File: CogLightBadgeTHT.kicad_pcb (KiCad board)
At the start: 2 copper layers, 87.4 x 123 mm, 28 parts, among them J1 AVR-ISP, SW1 SW_SPDT, SW2 SW_Push, SW3 SW_Push, U1 ATtiny84A-PU

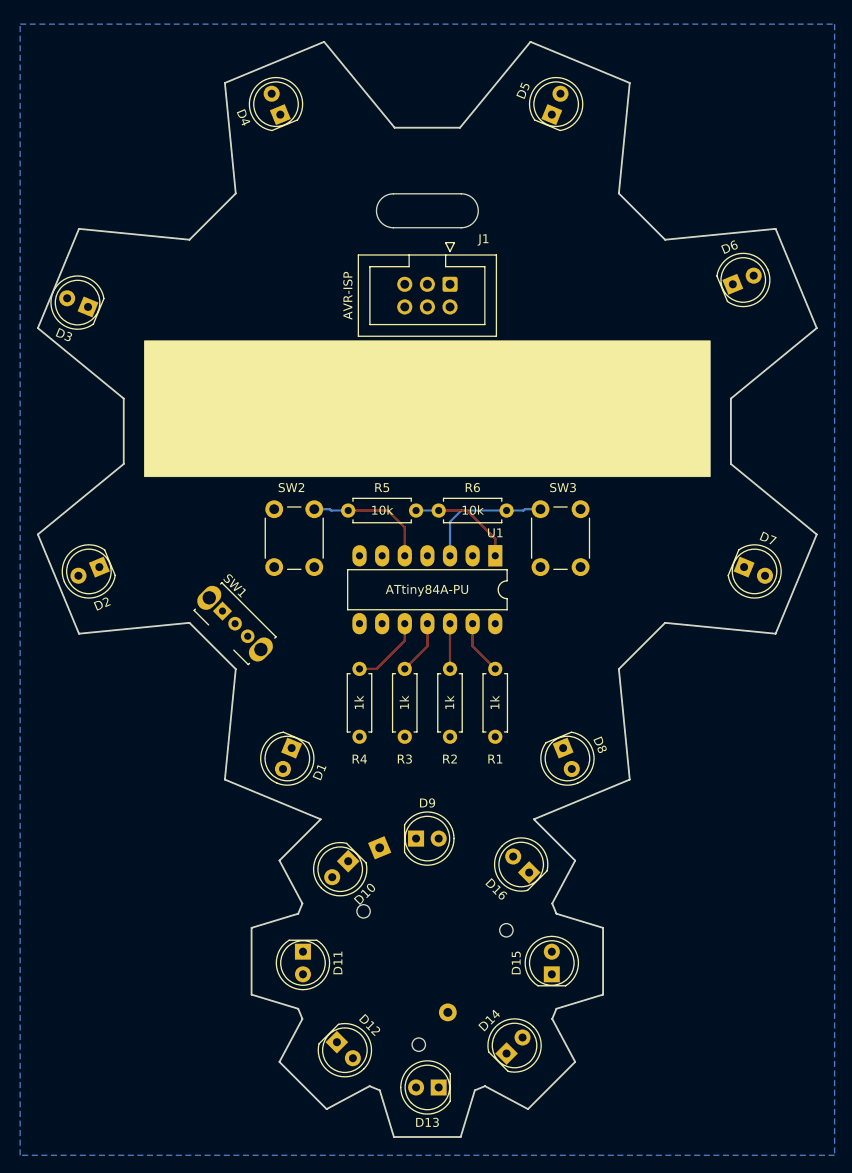
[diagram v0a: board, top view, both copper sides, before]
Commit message: Downsized pcb and component layout
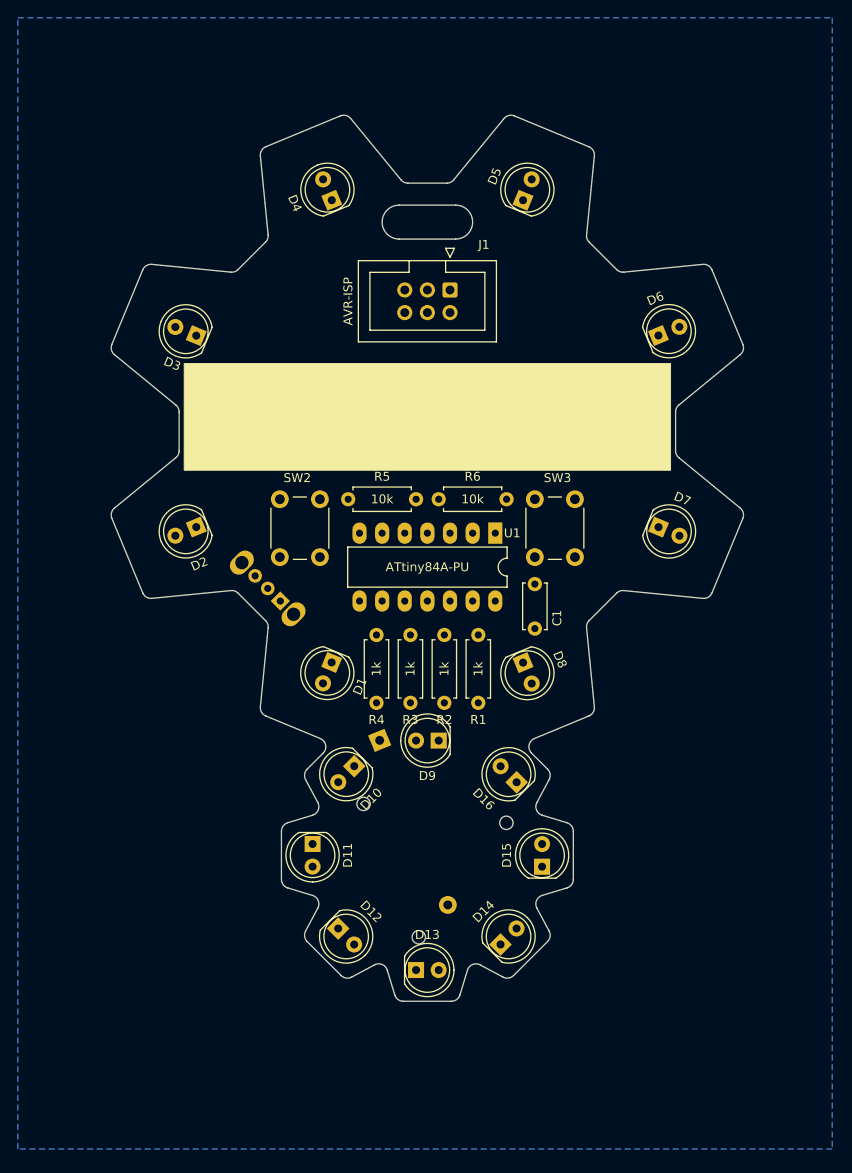
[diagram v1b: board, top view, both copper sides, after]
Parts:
- added C1: 100nF, Capacitor_THT:C_Disc_D5.0mm_W2.5mm_P5.00mm, F.Cu at (88.3, 93.3)
- SW1: moved to B.Cu
- moved D13 13.4 mm to (74.9, 136.7), turned to 0 degrees
- moved D12 12.8 mm to (66.2, 132.0)
- moved D3 12.6 mm to (50.2, 65.5)
- moved D14 12.3 mm to (84.4, 133.8)
- moved D11 12.1 mm to (63.3, 122.5)
- moved D15 12.1 mm to (89.1, 125.1)
- moved BT1 12.1 mm to (76.2, 123.8)
- moved D2 11.8 mm to (50.3, 86.9)
- moved D9 11.3 mm to (77.5, 110.9), turned to 180 degrees
- moved D4 11.2 mm to (65.5, 50.3)
- moved D10 10.7 mm to (68.0, 113.8)
- moved D1 10.6 mm to (65.5, 102.1)
- moved D7 10.6 mm to (102.2, 87.0)
- moved D8 10.6 mm to (86.9, 102.2)
- moved D16 10.2 mm to (86.2, 115.6)
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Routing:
- net Net-(R6-Pad2): track 14.6 -> 0.00 mm
- net Net-(R5-Pad2): track 14.2 -> 0.00 mm
- net VCC: track 12.1 -> 0.00 mm
- net /source4: track 8.30 -> 0.00 mm
- net /source3: track 6.13 -> 0.00 mm
- net /source1: track 6.13 -> 0.00 mm
- net /source2: track 5.08 -> 0.00 mm
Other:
- board size 87.4 x 123 mm -> 71 x 99.5 mm

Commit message: Trace routing
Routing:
- net /sink3: track 0.00 -> 159.2 mm, vias 0 -> 8
- net /sink2: track 0.00 -> 144.8 mm, vias 0 -> 3
- net /sink4: track 0.00 -> 126.9 mm, vias 0 -> 1
- net /sink1: track 0.00 -> 120.5 mm, vias 0 -> 4
- net Net-(D1-Pad2): track 0.00 -> 97.7 mm, vias 0 -> 1
- net Net-(D5-Pad2): track 0.00 -> 84.6 mm
- net VCC: track 0.00 -> 65.3 mm
- net Net-(D13-Pad2): track 0.00 -> 55.9 mm
- net Net-(D10-Pad2): track 0.00 -> 39.8 mm
- net Net-(J1-Pad5): track 0.00 -> 30.0 mm
- net Net-(BT1-Pad1): track 0.00 -> 27.6 mm
- net Net-(R6-Pad2): track 0.00 -> 18.7 mm
- net Net-(R5-Pad2): track 0.00 -> 18.7 mm
- net /source4: track 0.00 -> 5.87 mm
- net /source3: track 0.00 -> 4.60 mm
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
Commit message: Improved siklscreen layout
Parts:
- C1: value 100nF -> .1uF

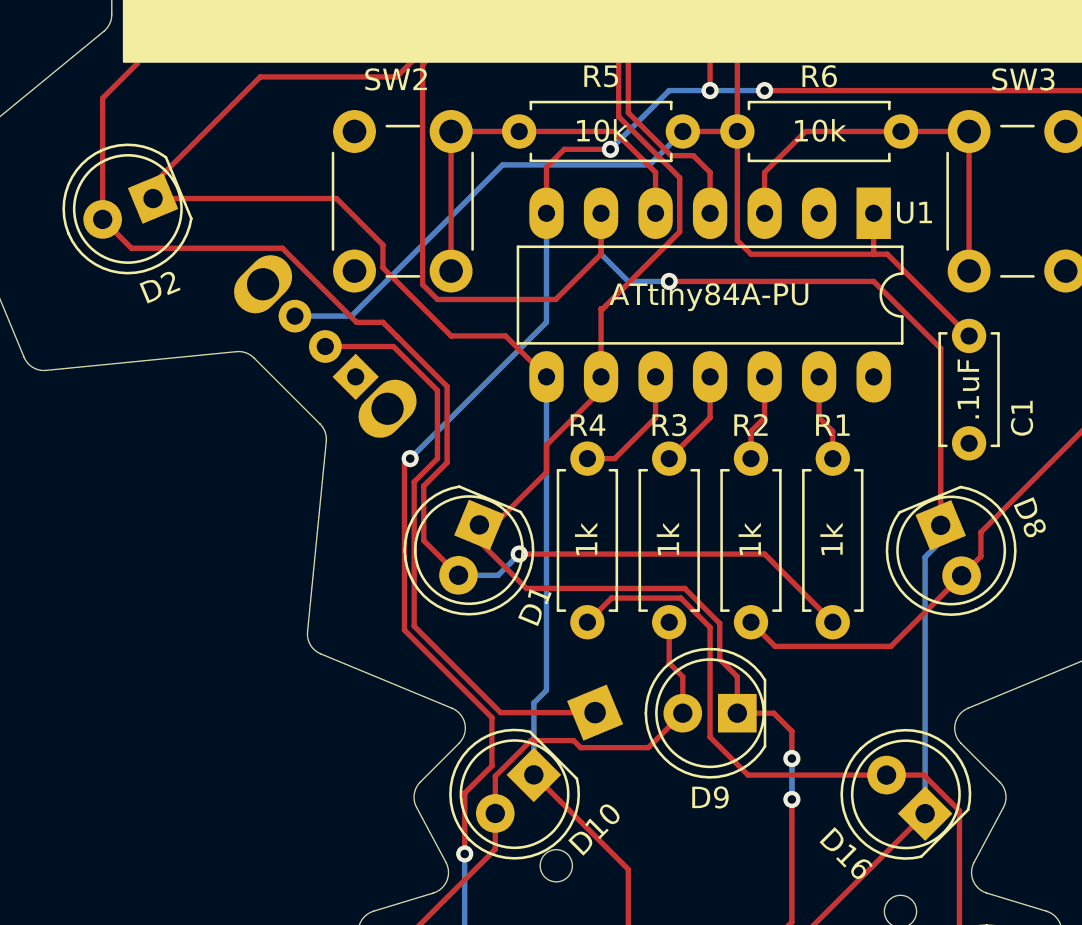
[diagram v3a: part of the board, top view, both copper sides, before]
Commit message: Removing sharp angles connecting angled square pads
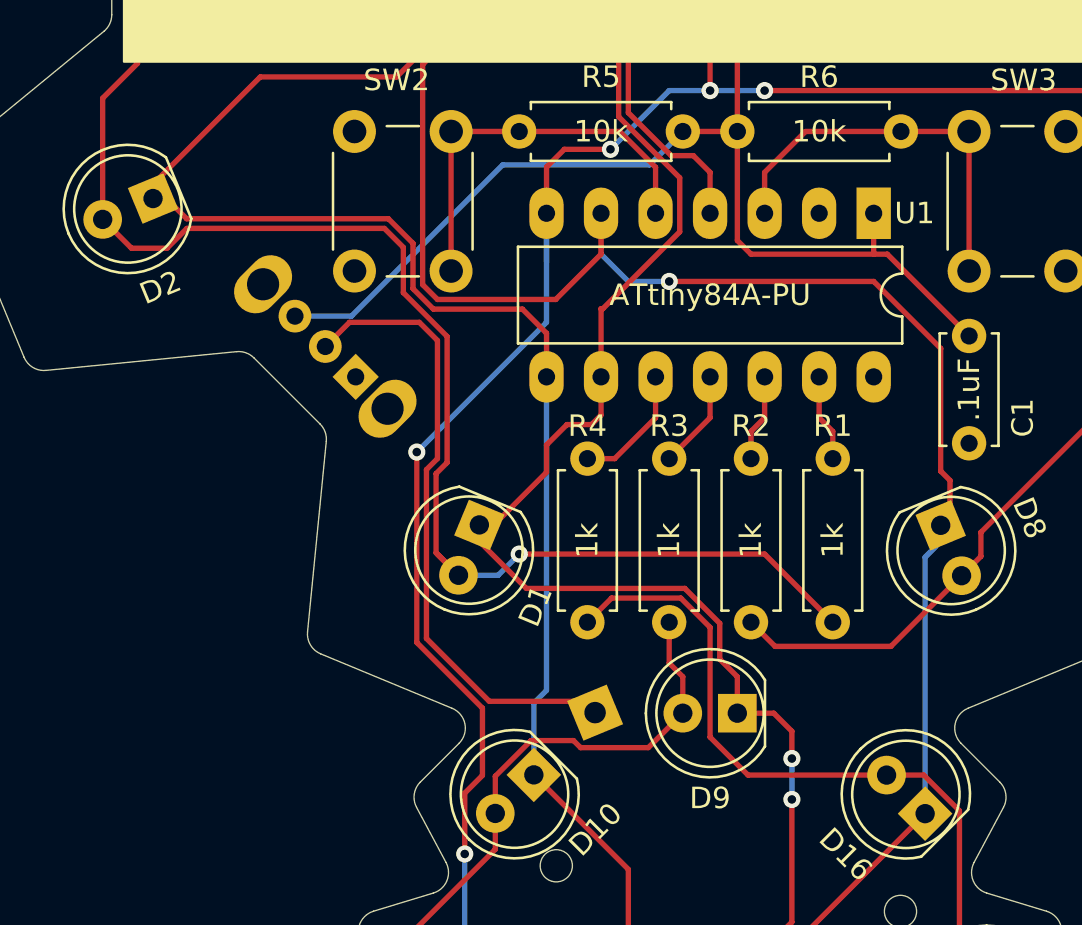
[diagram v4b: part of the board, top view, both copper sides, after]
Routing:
- net Net-(D1-Pad2): track 97.7 -> 102.0 mm
- net Net-(BT1-Pad1): track 27.6 -> 29.4 mm
- net /sink2: track 144.8 -> 146.6 mm
- net /sink3: track 159.2 -> 160.6 mm
- net /sink1: track 120.5 -> 121.2 mm

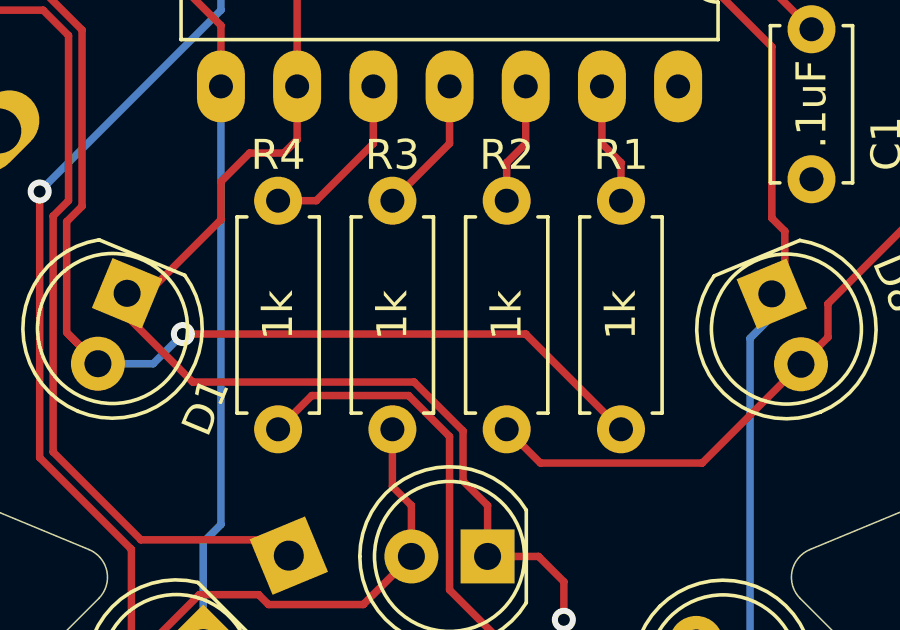
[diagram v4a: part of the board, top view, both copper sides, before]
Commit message: Changing LED resistors to 330 ohm
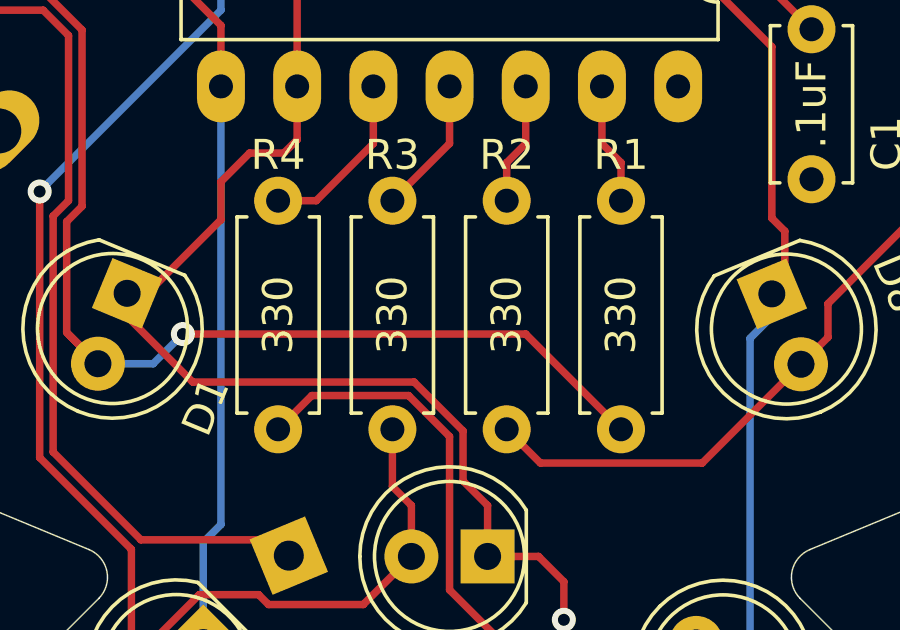
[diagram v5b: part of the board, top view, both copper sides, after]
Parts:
- R1, R2, R3, R4: value 1k -> 330
